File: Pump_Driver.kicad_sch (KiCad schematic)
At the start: 5 parts, among them J17 Conn_01x02, Q5 AO3400A

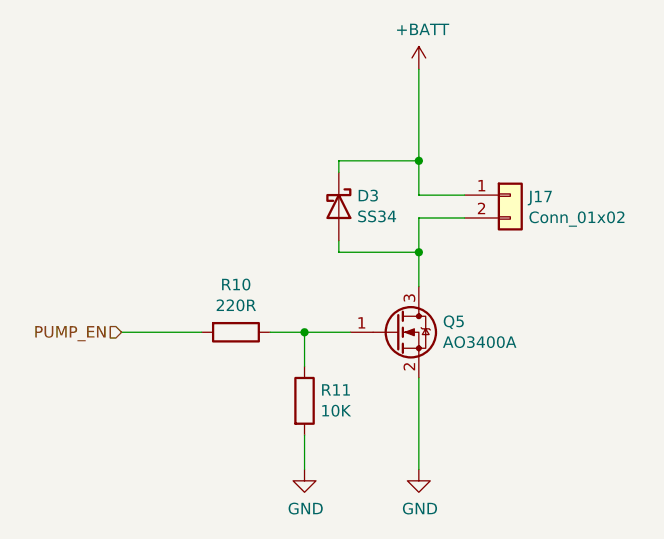
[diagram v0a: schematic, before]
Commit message: Move to KiCad v6, redesign circuit for chamber
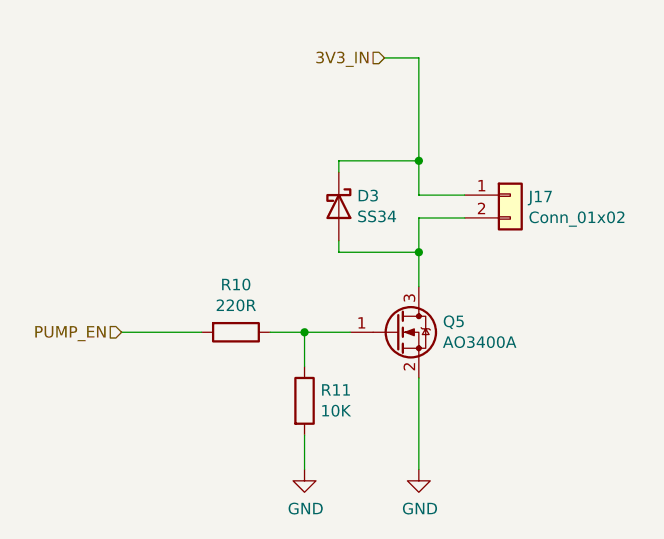
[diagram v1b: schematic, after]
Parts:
- J17: LCSC (none) -> C474881
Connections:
- net +BATT renamed 3V3_IN
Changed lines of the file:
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@@
+    (stroke (width 0) (type default) (color 0 0 0 0))
+  )
+  (wire (pts (xy 149.86 77.47) (xy 153.67 77.47))
     (stroke (width 0) (type default) (color 0 0 0 0))
   )
@@
     (stroke (width 0) (type default) (color 0 0 0 0))
   )
-  (wire (pts (xy 153.67 78.74) (xy 153.67 88.9))
+  (wire (pts (xy 153.67 77.47) (xy 153.67 88.9))
     (stroke (width 0) (type default) (color 0 0 0 0))
   )
@@
   )
   (hierarchical_label "PUMP_EN" (shape input) (at 120.65 107.95 180)
+    (effects (font (size 1.27 1.27)) (justify right))
+  )
+  (hierarchical_label "3V3_IN" (shape input) (at 149.86 77.47 180)
     (effects (font (size 1.27 1.27)) (justify right))
   )
@@
     (pin "2")
   )
-  (symbol (lib_id "power:+BATT") (at 153.67 78.74 0) (unit 1)
-    (in_bom yes) (on_board yes)
-    (property "Reference" "#PWR040" (id 0) (at 153.67 82.55 0)
-      (effects (font (size 1.27 1.27)) hide)
-    )
-    (property "Value" "+BATT" (id 1) (at 154.051 74.3458 0))
-    (property "Footprint" "" (id 2) (at 153.67 78.74 0)
-      (effects (font (size 1.27 1.27)) hide)
-    )
-    (property "Datasheet" "" (id 3) (at 153.67 78.74 0)
-      (effects (font (size 1.27 1.27)) hide)
-    )
-    (pin "1")
-  )
   (symbol (lib_id "Connector_Generic:Conn_01x02") (at 163.83 92.71 0) (unit 1)
     (in_bom yes) (on_board yes)
@@
       (effects (font (size 1.27 1.27)) hide)
     )
+    (property "LCSC" "C474881" (id 4) (at 163.83 92.71 0)
+      (effects (font (size 1.27 1.27)) hide)
+    )

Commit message: Add test points, add JLC part numbers to JST XH connectors, clean up
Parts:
- J17: footprint Connector_JST:JST_XH_B2B-XH-AM_1x02_P2.50mm_Vertical -> co2_sensor_node:KF301-5.0-2P
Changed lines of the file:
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@@
       (effects (font (size 1.27 1.27)) (justify left))
     )
-    (property "Footprint" "Connector_JST:JST_XH_B2B-XH-AM_1x02_P2.50mm_Vertical" (id 2) (at 163.83 92.71 0)
+    (property "Footprint" "co2_sensor_node:KF301-5.0-2P" (id 2) (at 163.83 92.71 0)
       (effects (font (size 1.27 1.27)) hide)
     )

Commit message: Finalize schematic
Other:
- title: (none) -> CO2 Chamber - Pump Driver
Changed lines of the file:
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@@
 (kicad_sch (version 20211123) (generator eeschema)
   (paper "A4")
+  (title_block
+    (title "CO2 Chamber - Pump Driver")
+    (date "2022-05-20")
+    (rev "1")
+  )
   (junction (at 153.67 99.06) (diameter 0) (color 0 0 0 0)
   )
